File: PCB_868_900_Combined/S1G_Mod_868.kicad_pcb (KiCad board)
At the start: 4 copper layers, 60 x 27 mm, 78 parts, among them J2 20021121-00010C4LF, J5 0475890001-MicroUSBPort, P1 CONN_02X08, Q1 DMG2307L-7, SW1 CUS-12TB, SW2 B3U-1000P, T1 0732511150, U1 AP7361-33FGE-7, U2 ADF7023BCPZ, U3 STM32L052C8T6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

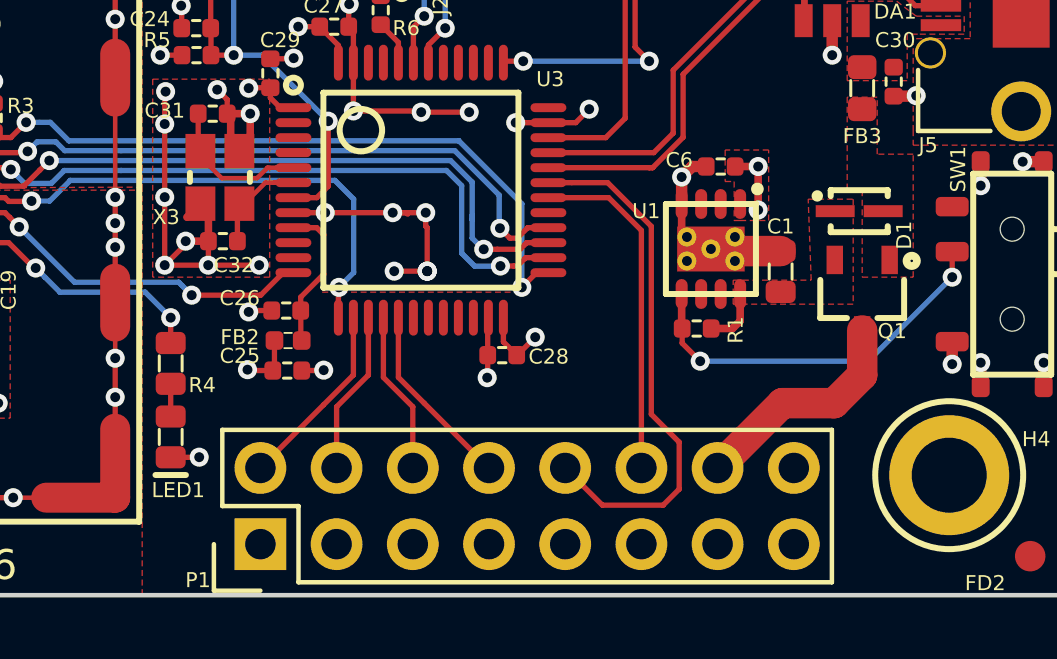
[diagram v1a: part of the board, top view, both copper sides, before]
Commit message: PCBs Tweaked A lot
PCBs have been tweaked. The separate implementation has been finished
but also has GPIOs from the MCU broken out to the connector, same for
the combined implementation. Both boards now have power indication LEDs
(red).
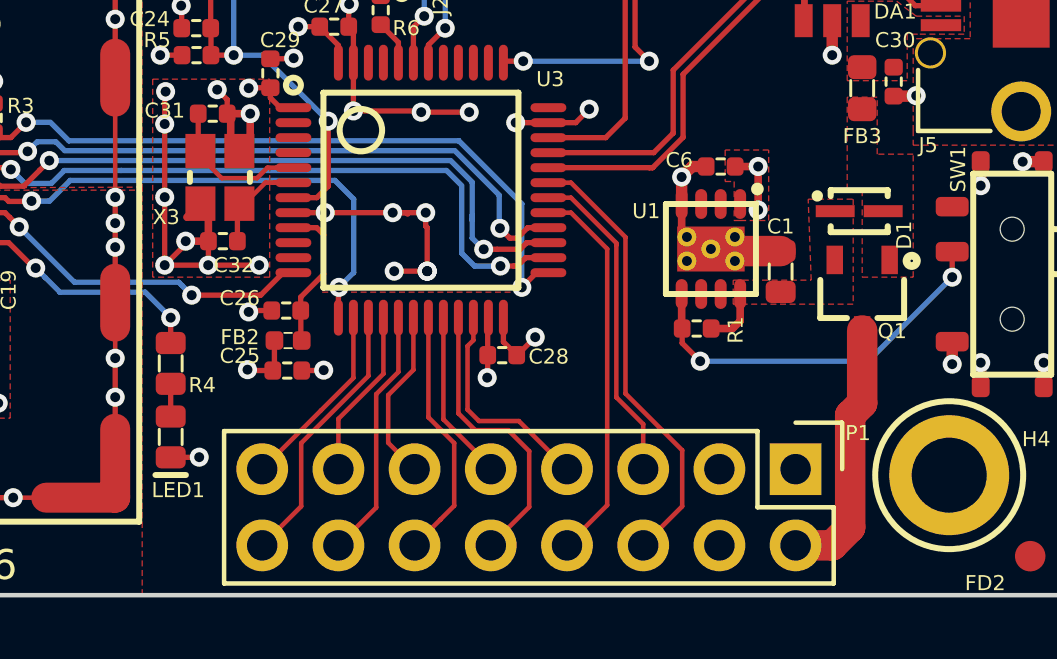
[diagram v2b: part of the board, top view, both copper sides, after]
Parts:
- moved P1 18.0 mm to (107.4, 60.8), turned to 270 degrees
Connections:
- P1 pad 1: Net-(P1-Pad1) -> GND
- P1 pad 10: /MCU - STM32L052K8T6/USART1_RX -> /MCU - STM32L052K8T6/GPIO_PB10
- P1 pad 11: Net-(P1-Pad11) -> /MCU - STM32L052K8T6/GPIO_PB0
- P1 pad 12: /MCU - STM32L052K8T6/USART1_TX -> /MCU - STM32L052K8T6/GPIO_PB1
- P1 pad 13: Net-(P1-Pad13) -> /MCU - STM32L052K8T6/SPI2_MISO
- P1 pad 14: /PSU_IN -> /MCU - STM32L052K8T6/SPI2_MOSI
- P1 pad 15: GND -> /MCU - STM32L052K8T6/SPI2_NSS
- P1 pad 16: GND -> /MCU - STM32L052K8T6/SPI2_SCLK
- P1 pad 2: /MCU - STM32L052K8T6/SPI2_NSS -> /PSU_IN
- P1 pad 4: /MCU - STM32L052K8T6/SPI2_SCLK -> Net-(P1-Pad4)
- P1 pad 5: Net-(P1-Pad5) -> /MCU - STM32L052K8T6/USART1_TX
- P1 pad 6: /MCU - STM32L052K8T6/SPI2_MISO -> /MCU - STM32L052K8T6/USART1_RX
- P1 pad 7: Net-(P1-Pad7) -> /MCU - STM32L052K8T6/GPIO_PB11
- P1 pad 8: /MCU - STM32L052K8T6/SPI2_MOSI -> /MCU - STM32L052K8T6/GPIO_PA8
- P1 pad 9: Net-(P1-Pad9) -> /MCU - STM32L052K8T6/GPIO_PB2
- U3 pad 18: Net-(U3-Pad18) -> /MCU - STM32L052K8T6/GPIO_PB0
- U3 pad 19: Net-(U3-Pad19) -> /MCU - STM32L052K8T6/GPIO_PB1
- U3 pad 20: Net-(U3-Pad20) -> /MCU - STM32L052K8T6/GPIO_PB2
- U3 pad 21: Net-(U3-Pad21) -> /MCU - STM32L052K8T6/GPIO_PB10
- U3 pad 22: Net-(U3-Pad22) -> /MCU - STM32L052K8T6/GPIO_PB11
- U3 pad 29: Net-(U3-Pad29) -> /MCU - STM32L052K8T6/GPIO_PA8
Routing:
- net /MCU - STM32L052K8T6/GPIO_PA8: track 0.00 -> 12.9 mm
- net /MCU - STM32L052K8T6/GPIO_PB10: track 0.00 -> 9.74 mm
- net /MCU - STM32L052K8T6/GPIO_PB1: track 0.00 -> 8.49 mm
- net /MCU - STM32L052K8T6/GPIO_PB11: track 0.00 -> 7.28 mm
- net /MCU - STM32L052K8T6/GPIO_PB0: track 0.00 -> 5.76 mm
- net /MCU - STM32L052K8T6/GPIO_PB2: track 0.00 -> 5.70 mm
- net /MCU - STM32L052K8T6/SPI2_SCLK: track 5.45 -> 9.06 mm
- net /MCU - STM32L052K8T6/USART1_RX: track 17.7 -> 14.9 mm
- net /MCU - STM32L052K8T6/SPI2_MOSI: track 6.26 -> 8.42 mm
- net /PSU_IN: track 7.59 -> 8.80 mm
- net /MCU - STM32L052K8T6/USART1_TX: track 11.5 -> 10.8 mm

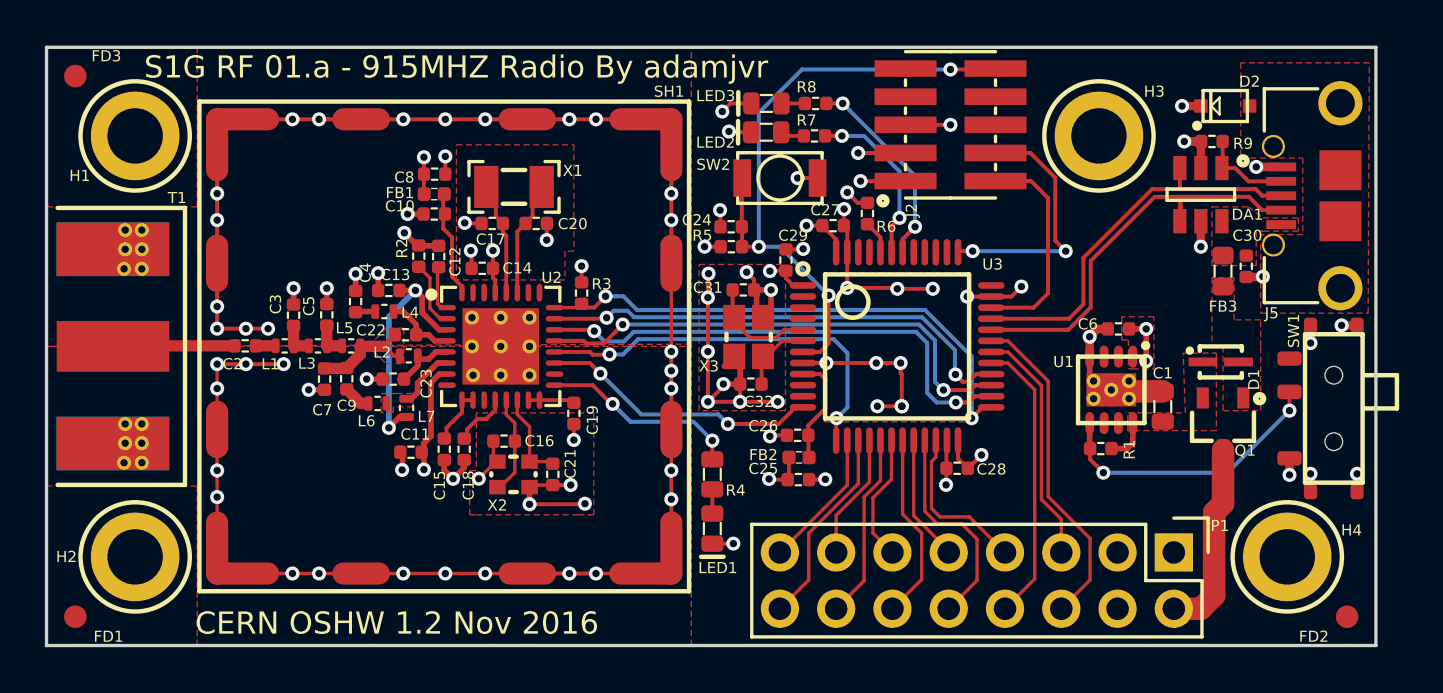
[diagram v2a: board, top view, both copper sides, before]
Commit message: Grounding and Adapter
Grounding changed on both versions of the 915MHZ/868MHZ versions of the
radio both the combined and separate antenna versions. Also an adapter
is being developed for alternative connection options.
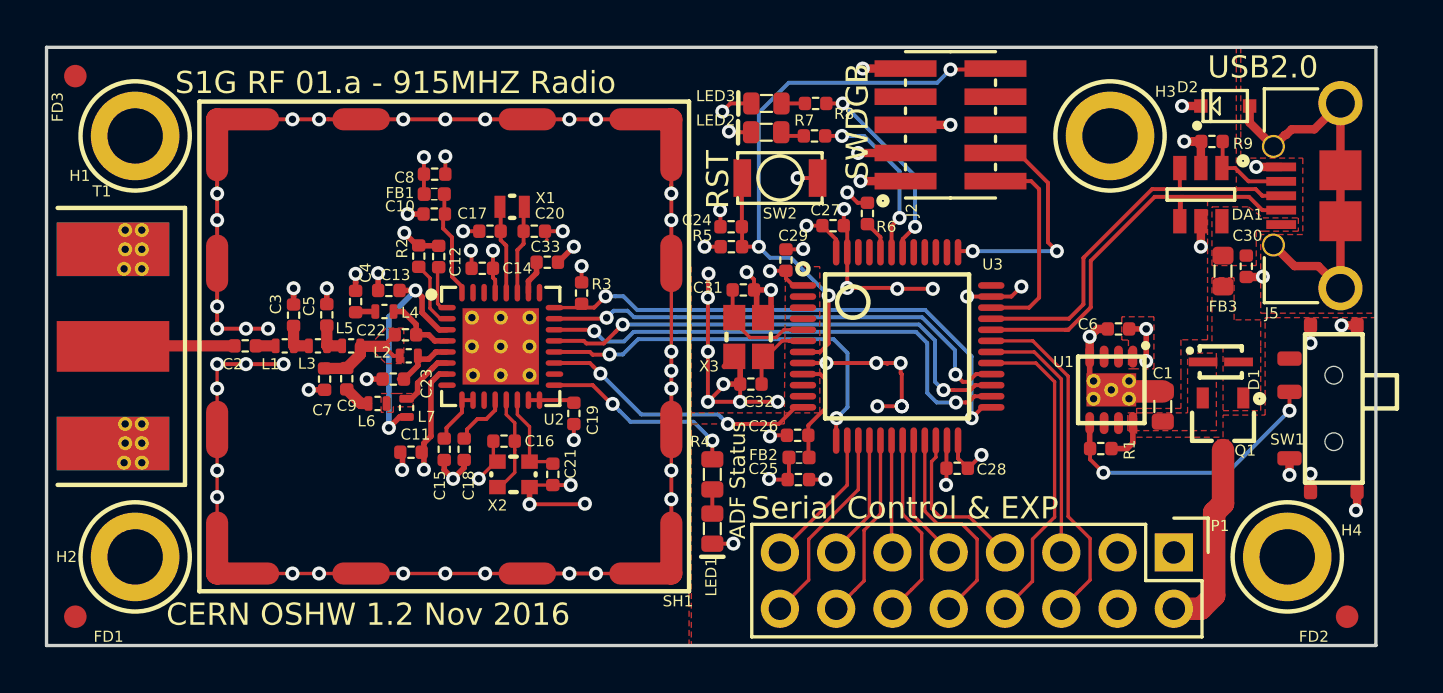
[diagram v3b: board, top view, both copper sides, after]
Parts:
- added C33: CL10B224JO8NNNC, PCB_Footprints:C0402, F.Cu at (79.1, 47.7)
- C17, C20: value CL05C180GB5NCNC -> CL05C090CB5NNNC
- X1: value ABS07-32.768KHZ-9-T -> ABS05-32.768KHZ-9-T; footprint PCB_Footprints:ABS07-32.768KHZ-9-T -> PCB_Footprints:ABS05-32.768KHZ-9-T
- moved X1 0.90 mm to (77.5, 45.2)
- moved H3 0.50 mm to (104.5, 42.0)
- moved C17 0.36 mm to (76.5, 46.3), turned to 0 degrees
- moved C20 0.36 mm to (78.5, 46.3)
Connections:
- C17 pad 1: Net-(C17-Pad1) -> GND
- C17 pad 2: GND -> Net-(C17-Pad2)
- U2 pad 28: Net-(C17-Pad1) -> Net-(C17-Pad2)
- X1 pad 1: Net-(C17-Pad1) -> Net-(C17-Pad2)
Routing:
- net Net-(D2-Pad1): track 0.00 -> 18.3 mm
- net Net-(C17-Pad1): track 5.15 -> 0.00 mm
- net Net-(C17-Pad2): track 0.00 -> 4.00 mm
- net GND: track 165.3 -> 168.3 mm, vias 96 -> 98
- net Net-(C33-Pad1): track 0.00 -> 1.53 mm
- net /MCU - STM32L052K8T6/GPIO_PA8: track 12.9 -> 14.4 mm
- net Net-(C20-Pad1): track 5.23 -> 4.01 mm
- net /MCU - STM32L052K8T6/SWCLK: track 12.6 -> 11.7 mm
- net /MCU - STM32L052K8T6/USART1_TX: track 10.8 -> 11.5 mm
- net /MCU - STM32L052K8T6/GPIO_PB0: track 5.76 -> 5.07 mm
- net /MCU - STM32L052K8T6/USART1_RX: track 14.9 -> 15.6 mm
- added copper zone on B.Cu, net GND
- added copper zone on In2.Cu, net GND
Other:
- board text added: "ADF Status"
- board text added: "OFF"
- board text added: "ON"
- board text added: "RST"
- board text added: "S1G RF 01.a - 915MHZ Radio"
- board text added: "S1G RF 01.a - 915MHZ Radio CERN OSHW 1.2 Nov 2016 Designed by Adam Vadala-Roth https://github.com/adamjvr/S1G-Mod"
- board text added: "SWDGB"
- board text added: "Serial Control & EXP"
- board text added: "USB2.0"
- board text removed: "S1G RF 01.a - 915MHZ Radio By adamjvr"

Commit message: Via Stitching
Ground pour stiching applied to the combined PA/LNA match version of the
915MHZ radio. All ground pours and layers are now stiched together
effectively.
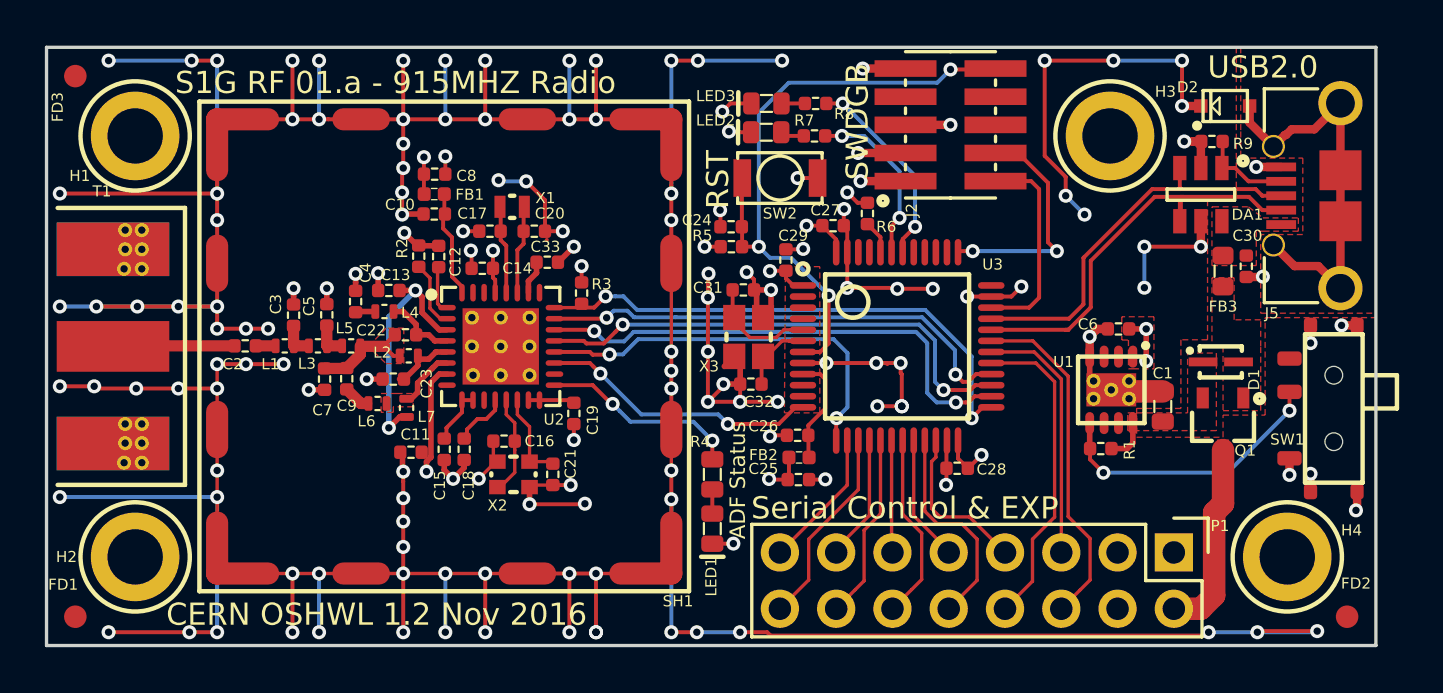
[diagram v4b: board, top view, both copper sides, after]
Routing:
- net GND: track 168.3 -> 343.7 mm, vias 98 -> 153
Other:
- board text added: "CERN OSHWL 1.2 Nov 2016"
- board text removed: "CERN OSHW 1.2 Nov 2016"

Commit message: Additional GPIO
Two additional GPIO pins from the STM32L0 have been added to the
connector, now there is a signal on every pin. The connector component
has been replaced with one that has a STEP 3D model for proper 3D model
exporting from KiCAD for enclosure design. This has been done to both
versions of the radio.
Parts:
- P1: value CONN_02X08 -> 61301621121; footprint Pin_Headers:Pin_Header_Straight_2x08 -> PCB_Footprints:61301621121
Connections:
- P1 pad 3: Net-(P1-Pad3) -> /MCU - STM32L052K8T6/GPIO_PA15
- P1 pad 4: Net-(P1-Pad4) -> /MCU - STM32L052K8T6/GPIO_PB3
- U3 pad 38: Net-(U3-Pad38) -> /MCU - STM32L052K8T6/GPIO_PA15
- U3 pad 39: Net-(U3-Pad39) -> /MCU - STM32L052K8T6/GPIO_PB3
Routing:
- net /MCU - STM32L052K8T6/GPIO_PB3: track 0.00 -> 31.0 mm, vias 0 -> 2
- net /MCU - STM32L052K8T6/GPIO_PA15: track 0.00 -> 26.8 mm, vias 0 -> 2
- net GND: track 343.7 -> 344.8 mm, vias 153 -> 152

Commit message: Adapters
Adapter ended up being too large. So I split it into two separate
adapters one for SPI and one for USART over JST connectors. SPI board
has 100 ohm inline resistors for EMI and impedance matching in case the
driving device lacks these internally or on its board.  Additional
Fudicials added to the combined implementation.
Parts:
- added FD4: FIDUCIAL, PCB_Footprints:FIDUCIAL, B.Cu at (115.2, 63.7)
- added FD5: FIDUCIAL, PCB_Footprints:FIDUCIAL, B.Cu at (57.8, 39.3)
- added FD6: FIDUCIAL, PCB_Footprints:FIDUCIAL, B.Cu at (57.8, 63.7)
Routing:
- net GND: track 344.8 -> 359.6 mm, vias 152 -> 157
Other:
- board text added: "S1G-RF 01.a - 915MHZ Radio"
- board text removed: "S1G RF 01.a - 915MHZ Radio"
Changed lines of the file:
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@@
   (general
     (links 226)
-    (no_connects 3)
+    (no_connects 1)
     (area 56.424999 37.924999 116.575001 65.075001)
     (thickness 1.6)
     (drawings 15)
-    (tracks 900)
+    (tracks 913)
     (zones 0)
-    (modules 79)
-    (nets 98)
+    (modules 82)
+    (nets 101)
   )
   (page A4)
@@
     (34 B.Paste user)
     (35 F.Paste user)
-    (36 B.SilkS user hide)
+    (36 B.SilkS user)
     (37 F.SilkS user)
     (38 B.Mask user)
@@
   (net 96 "/MCU - STM32L052K8T6/GPIO_PA15")
   (net 97 "/MCU - STM32L052K8T6/GPIO_PB3")
+  (net 98 "Net-(FD6-Pad1)")
+  (net 99 "Net-(FD5-Pad1)")
+  (net 100 "Net-(FD4-Pad1)")
   (net_class Default "This is the default net class."
     (clearance 0.1524)
@@
     (add_net "Net-(FD2-Pad1)")
     (add_net "Net-(FD3-Pad1)")
+    (add_net "Net-(FD4-Pad1)")
+    (add_net "Net-(FD5-Pad1)")
+    (add_net "Net-(FD6-Pad1)")
     (add_net "Net-(H1-Pad1)")
     (add_net "Net-(H2-Pad1)")
@@
     (add_net "Net-(U3-Pad46)")
   )
+  (module PCB_Footprints:FIDUCIAL (layer B.Cu)
+    (at 115.2 63.7)
+    (clearance 0.508)
+    (fp_text reference FD4 (at -1.85 -0.05) (layer B.SilkS)
+      (effects (font (size 0.5 0.5) (thickness 0.1)) (justify mirror))
+    )
+    (fp_text value FIDUCIAL (at 0 3.048) (layer B.Fab)
+      (effects (font (size 0.5 0.5) (thickness 0.1)) (justify mirror))
+    )
+    (pad 1 smd circle (at 0 0) (size 1.016 1.016) (layers B.Cu B.Mask)
+      (net 100 "Net-(FD4-Pad1)") (solder_mask_margin 0.508))
+  )
+  (module PCB_Footprints:FIDUCIAL (layer B.Cu)
+    (at 57.8 39.3)
+    (clearance 0.508)
+    (fp_text reference FD5 (at 1.875 0.025) (layer B.SilkS)
+      (effects (font (size 0.5 0.5) (thickness 0.1)) (justify mirror))
+    )
+    (fp_text value FIDUCIAL (at 0 3.048) (layer B.Fab)
+      (effects (font (size 0.5 0.5) (thickness 0.1)) (justify mirror))
+    )
+    (pad 1 smd circle (at 0 0) (size 1.016 1.016) (layers B.Cu B.Mask)
+      (net 99 "Net-(FD5-Pad1)") (solder_mask_margin 0.508))
+  )
+  (module PCB_Footprints:FIDUCIAL (layer B.Cu)
+    (at 57.8 63.7)
+    (clearance 0.508)
+    (fp_text reference FD6 (at 2.05 0.025) (layer B.SilkS)
+      (effects (font (size 0.5 0.5) (thickness 0.1)) (justify mirror))
+    )
+    (fp_text value FIDUCIAL (at 0 3.048) (layer B.Fab)
+      (effects (font (size 0.5 0.5) (thickness 0.1)) (justify mirror))
+    )
+    (pad 1 smd circle (at 0 0) (size 1.016 1.016) (layers B.Cu B.Mask)
+      (net 98 "Net-(FD6-Pad1)") (solder_mask_margin 0.508))
+  )
   (module PCB_Footprints:61301621121 (layer F.Cu)
     (at 107.38 60.8 270)
@@
     (tags "pin header")
     (fp_text reference P1 (at 2.25 -2.12 270) (layer F.SilkS)
-      (effects (font (size 1 1) (thickness 0.15)))
+      (effects (font (size 0.5 0.5) (thickness 0.1)))
     )
     (fp_text value 61301621121 (at 0 19.85 270) (layer F.Fab)
-      (effects (font (size 1 1) (thickness 0.15)))
+      (effects (font (size 0.5 0.5) (thickness 0.1)))
     )
     (fp_line (start -1.55 -1.55) (end -1.55 0) (layer F.SilkS) (width 0.15))
@@
     (at 57.8 63.7)
     (clearance 0.635)
-    (fp_text reference FD1 (at -0.55 -1.45) (layer F.SilkS)
+    (fp_text reference FD1 (at -0.15 -1.825 90) (layer F.SilkS)
       (effects (font (size 0.5 0.5) (thickness 0.1)))
     )
@@
     (at 115.2 63.7)
     (clearance 0.635)
-    (fp_text reference FD2 (at 0.4 -1.5) (layer F.SilkS)
+    (fp_text reference FD2 (at 0.2 -1.875 90) (layer F.SilkS)
       (effects (font (size 0.5 0.5) (thickness 0.1)))
     )
@@
     (at 57.8 39.3)
     (clearance 0.635)
-    (fp_text reference FD3 (at -0.8 1.4 90) (layer F.SilkS)
+    (fp_text reference FD3 (at 1.85 -0.175 180) (layer F.SilkS)
       (effects (font (size 0.5 0.5) (thickness 0.1)))
     )
@@
   (module PCB_Footprints:M2.5_HOLE (layer F.Cu)
     (at 60.5 61)
-    (fp_text reference H2 (at -3.1 0) (layer F.SilkS)
+    (fp_text reference H2 (at 1.8 -2.45) (layer F.SilkS)
       (effects (font (size 0.5 0.5) (thickness 0.1)))
     )
@@
   )
   (gr_line (start 40 51.5) (end 120 51.5) (layer Dwgs.User) (width 0.15))
-  (gr_text "S1G RF 01.a - 915MHZ Radio\n" (at 62.3 39.6) (layer F.SilkS)
+  (gr_text "S1G-RF 01.a - 915MHZ Radio\n" (at 62.3 39.6) (layer F.SilkS)
     (effects (font (size 1 1) (thickness 0.18)) (justify left))
   )
@@
   (gr_line (start 56.5 65) (end 116.5 65) (layer Edge.Cuts) (width 0.15))
   (segment (start 79.083 46.692) (end 79.075 46.7) (width 0.1778) (layer F.Cu) (net 0))
+  (segment (start 115.6 58.9) (end 115.6 62.075) (width 0.1778) (layer F.Cu) (net 1))
+  (segment (start 115.6 62.075) (end 115.9 62.375) (width 0.1778) (layer F.Cu) (net 1))
+  (via (at 115.9 62.375) (size 0.635) (drill 0.3302) (layers F.Cu B.Cu) (net 1))
+  (segment (start 57.1 44.6) (end 57.1 40.6) (width 0.1778) (layer B.Cu) (net 1))
+  (via (at 57.1 40.6) (size 0.635) (drill 0.3302) (layers F.Cu B.Cu) (net 1))
+  (segment (start 57.1 58.3) (end 57.1 62.375) (width 0.1778) (layer F.Cu) (net 1))
+  (via (at 57.1 62.375) (size 0.635) (drill 0.3302) (layers F.Cu B.Cu) (net 1))
+  (segment (start 83.6 46.75) (end 83.6 48.35) (width 0.1778) (layer F.Cu) (net 1))
+  (segment (start 83.6 48.35) (end 83.575 48.375) (width 0.1778) (layer F.Cu) (net 1))
+  (via (at 83.575 48.375) (size 0.635) (drill 0.3302) (layers F.Cu B.Cu) (net 1))
+  (segment (start 84.7 45.8) (end 84.55 45.8) (width 0.1778) (layer B.Cu) (net 1))
+  (segment (start 84.55 45.8) (end 83.6 46.75) (width 0.1778) (layer B.Cu) (net 1))
+  (via (at 83.6 46.75) (size 0.635) (drill 0.3302) (layers F.Cu B.Cu) (net 1))
   (segment (start 103.682499 45.232501) (end 102.917499 44.467501) (width 0.1778) (layer B.Cu) (net 1))
   (segment (start 104 45.55) (end 103.682499 45.232501) (width 0.1778) (layer B.Cu) (net 1))
